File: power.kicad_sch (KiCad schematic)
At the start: 36 parts, among them IC1 STM32MP157AAB3, IC3 STC3117IJT, IC4 MCP73830T-2AAI_MYY, IC5 MT41K256M16TW-107_P, IC6 STPMIC1BPQR

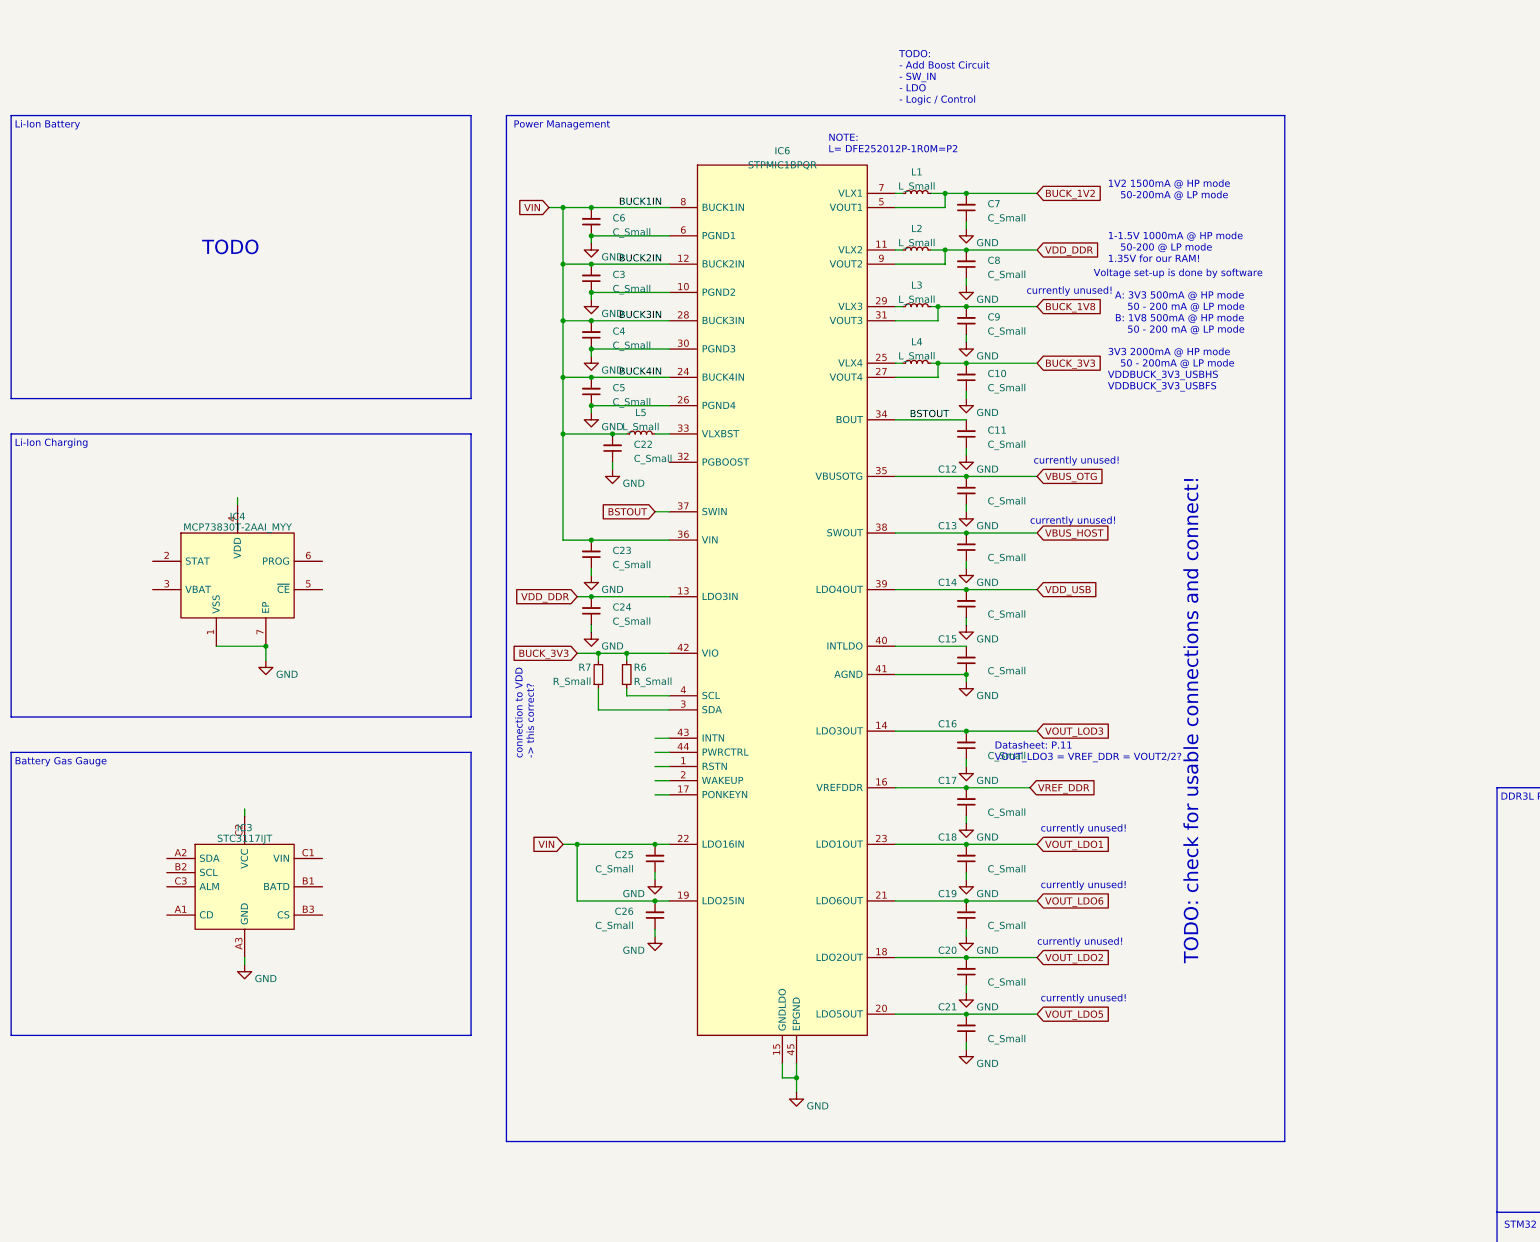
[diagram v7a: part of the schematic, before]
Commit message: Added gas gauge and Li-Ion charging
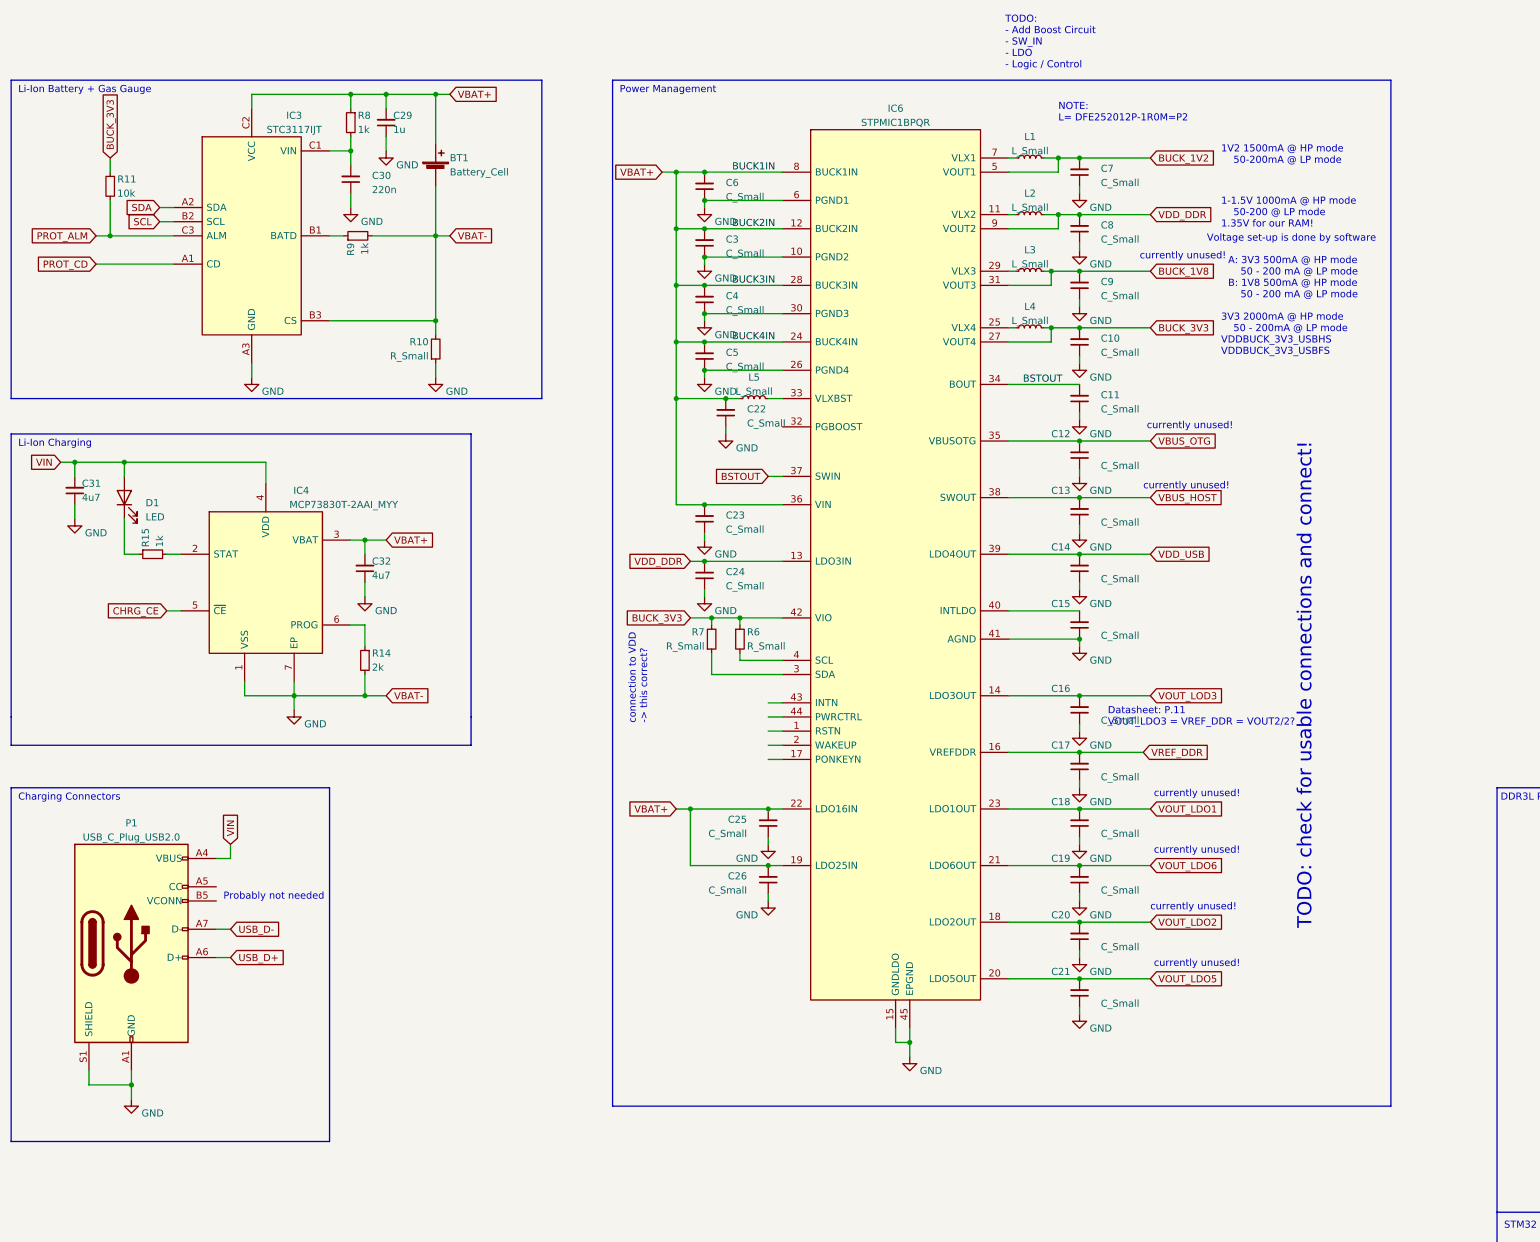
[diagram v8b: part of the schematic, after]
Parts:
- added BT1: Battery_Cell, symbol Device:Battery_Cell
- added C29: 1u, Capacitor_SMD:C_0603_1608Metric, symbol Device:C_Small
- added C30: 220n, Capacitor_SMD:C_0603_1608Metric, symbol Device:C_Small
- added C31, C32: 4u7, Capacitor_SMD:C_0603_1608Metric, symbol Device:C_Small
- added D1: LED, symbol Device:LED
- added P1: USB_C_Plug_USB2.0, symbol Connector:USB_C_Plug_USB2.0
- added R10: R_Small, symbol Device:R_Small
- added R11: 10k, Resistor_SMD:R_0603_1608Metric, symbol Device:R_Small
- added R14: 2k, Resistor_SMD:R_0603_1608Metric, symbol Device:R_Small
- added R15, R8, R9: 1k, Resistor_SMD:R_0603_1608Metric, symbol Device:R_Small
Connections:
- net BUCK_3V3: now also R11.1
- net GND: now also IC3.B3 (CS), BT1.2 (-), C29.1, C30.1, C31.1, C32.1, P1.A1 (GND), P1.A12 (GND), P1.B1 (GND), P1.B12 (GND), P1.S1 (SHIELD), R10.1, R10.2, R14.2, R9.2
- net VIN: now also IC4.4 (VDD), C31.2, D1.2 (A), P1.A4 (VBUS), P1.A9 (VBUS), P1.B4 (VBUS), P1.B9 (VBUS); no longer C22.2, C23.2, C25.2, C26.2, C3.2, C4.2, C5.2, C6.2, IC6.12 (BUCK2IN), IC6.19 (LDO25IN), IC6.22 (LDO16IN), IC6.24 (BUCK4IN), IC6.28 (BUCK3IN), IC6.36 (VIN), IC6.8 (BUCK1IN), L5.1
- net PROT_CD: now reaches IC3.A1 (CD)
- net SDA: now reaches IC3.A2 (SDA)
- net at IC3.B1 (BATD): now also R9.1
- net SCL: now reaches IC3.B2 (SCL)
- net at IC3.C1 (VIN): now also C30.2, R8.2
- net VBAT+: now reaches IC3.C2 (VCC)
- net VBAT+: now also C22.2, C23.2, C25.2, C26.2, C3.2, C4.2, C5.2, C6.2, IC4.3 (VBAT), IC6.12 (BUCK2IN), IC6.19 (LDO25IN), IC6.22 (LDO16IN), IC6.24 (BUCK4IN), IC6.28 (BUCK3IN), IC6.36 (VIN), IC6.8 (BUCK1IN), L5.1, BT1.1 (+), C29.2, C32.2, R8.1
- net PROT_ALM: now reaches IC3.C3 (ALM)
- net PROT_ALM: now also R11.2
- net at IC4.2 (STAT): now also R15.2
- net CHRG_CE: now reaches IC4.5 (~{CE})
- net at IC4.6 (PROG): now also R14.1
- new net: D1.1 (K), R15.1
- new net USB_D+: P1.A6 (D+)
- new net USB_D-: P1.A7 (D-)
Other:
- note added: "Charging Connectors"
- note added: "Li-Ion Battery + Gas Gauge"
- note added: "Probably not needed"
- note removed: "Battery Gas Gauge"
- note removed: "Li-Ion Battery"
- note removed: "TODO"
- moved on the sheet: C10, C11, C12, C13, C14, C15, C16, C17, C18, C19, C20, C21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
